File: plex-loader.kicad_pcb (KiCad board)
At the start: 2 copper layers, 38.1 x 68 mm, 42 parts, among them J1 Conn_01x05_Pin, J10 Conn_02x05_Odd_Even, J2 Conn_01x05_Pin, J3 Conn_01x05_Pin, J4 Conn_01x05_Pin, J5 Conn_01x05_Pin, J9 Conn_02x20_Odd_Even, U1 TMUX1208PWR, U2 TMUX1208PWR, U3 TMUX1208PWR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

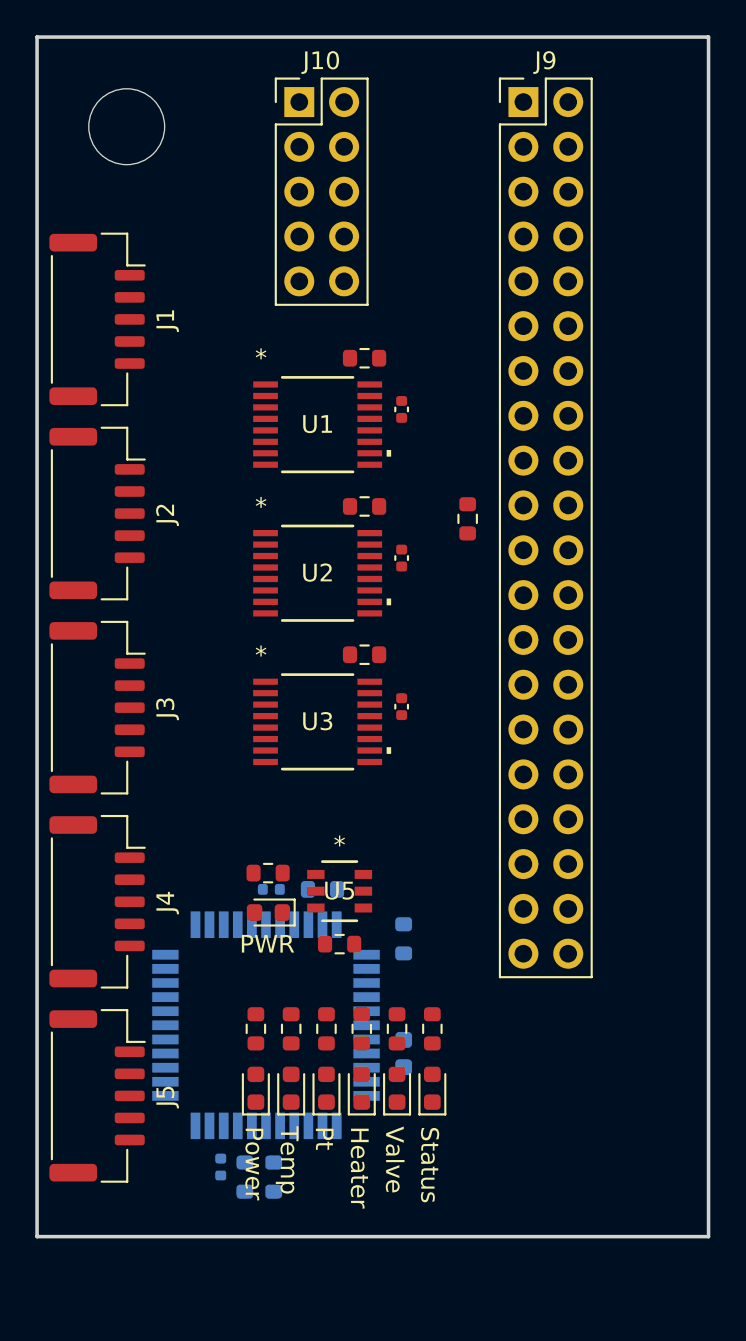
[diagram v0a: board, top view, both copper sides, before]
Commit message: switched footprint
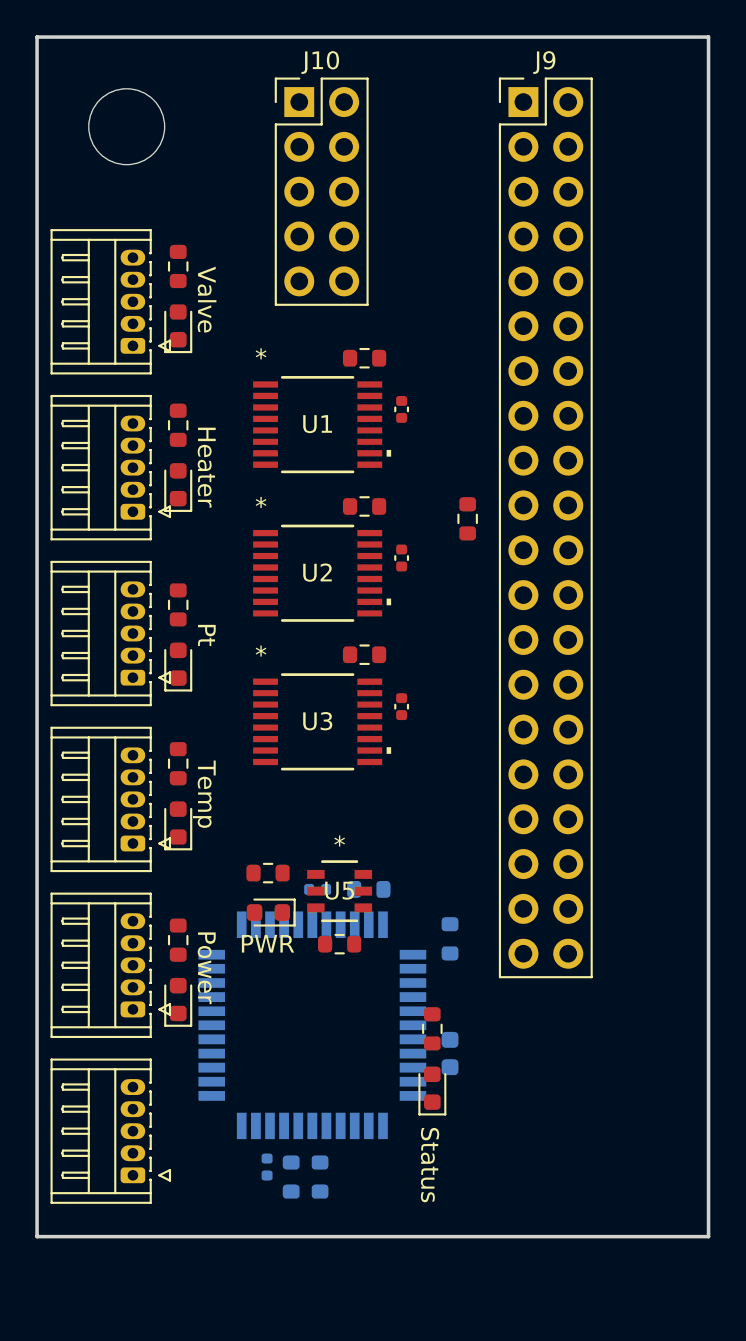
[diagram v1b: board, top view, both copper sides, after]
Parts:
- added J6: Conn_01x05_Pin, Connector_Hirose:Hirose_DF13-05P-1.25DS_1x05_P1.25mm_Horizontal, F.Cu at (55.4, 114.5)
- J1, J2, J3, J4, J5: footprint Connector_JST:JST_GH_SM05B-GHS-TB_1x05-1MP_P1.25mm_Horizontal -> Connector_Hirose:Hirose_DF13-05P-1.25DS_1x05_P1.25mm_Horizontal
- moved D3 44.9 mm to (58.0, 66.4)
- moved R12 44.9 mm to (58.0, 63.0)
- moved D4 35.7 mm to (58.0, 75.4)
- moved R13 35.7 mm to (58.0, 72.0)
- moved D5 25.5 mm to (58.0, 85.5)
- moved R14 25.5 mm to (58.0, 82.2)
- moved D6 16.3 mm to (58.0, 94.5)
- moved R15 16.3 mm to (58.0, 91.2)
- moved D7 6.68 mm to (58.0, 104.5)
- moved R16 6.68 mm to (58.0, 101.2)
- moved J5 5.30 mm to (55.4, 105.1), turned to 90 degrees
- moved J4 3.88 mm to (55.4, 95.7), turned to 90 degrees
- moved J3 2.65 mm to (55.4, 86.3), turned to 90 degrees
- moved C5 2.63 mm to (65.9, 98.3)
- moved R2 2.63 mm to (64.4, 114.6)
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
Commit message: update layers
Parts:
- added D8: LED, LED_SMD:LED_0603_1608Metric, F.Cu at (80.0, 105.6)
- added D9: LED, LED_SMD:LED_0603_1608Metric, F.Cu at (77.9, 105.6)
- added G***: LOGO, IMGS:etalogo, F.Cu at (69.0, 110.0)
- added R17: 50, Resistor_SMD:R_0603_1608Metric, F.Cu at (80.0, 108.8)
- added R18: 50, Resistor_SMD:R_0603_1608Metric, F.Cu at (77.9, 108.8)
- moved D2 15.0 mm to (58.0, 113.7)
- moved R11 15.0 mm to (58.0, 110.3)
- moved R3 2.01 mm to (69.2, 101.4)
- moved U5 2.01 mm to (69.2, 98.4)
- moved D1 2.01 mm to (65.1, 99.6)
- moved R4 2.01 mm to (65.1, 97.4)
- moved C1 1.10 mm to (71.8, 71.1)
- moved C2 1.10 mm to (71.8, 79.5)
- moved C3 1.10 mm to (71.8, 87.9)
- moved R7 1.10 mm to (69.7, 85.0)
- moved R8 1.10 mm to (69.7, 76.6)
- moved R9 1.10 mm to (69.7, 68.2)
- moved U1 1.10 mm to (67.0, 72.0)
- moved U2 1.10 mm to (67.0, 80.4)
- moved U3 1.10 mm to (67.0, 88.8)
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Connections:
- U4 pad 8: unconnected-(U4-PGED2/EMCD2/RP10/CN16/PMD2/RB10-Pad8) -> /dspic/B10
- U4 pad 9: unconnected-(U4-PGEC2/RP11/CN15/PMD1/RB11-Pad9) -> /dspic/B11
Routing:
- added copper zone on In2.Cu, net GND
- added copper zone on In1.Cu, net VDD
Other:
- copper layers 2 -> 4
- board text added: "Eta Space 2025 | Flash Upload Expansion Board V0"
- board text added: "Extra"
- board text added: "Status 1"
- board text added: "Status 2"
- board text removed: "Status"
